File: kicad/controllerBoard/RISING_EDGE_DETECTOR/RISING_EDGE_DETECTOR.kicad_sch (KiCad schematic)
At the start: 10 parts, among them Q385 PMOS, Q386 NMOS, Q391 PMOS, Q392 NMOS, Q393 PMOS, Q394 NMOS

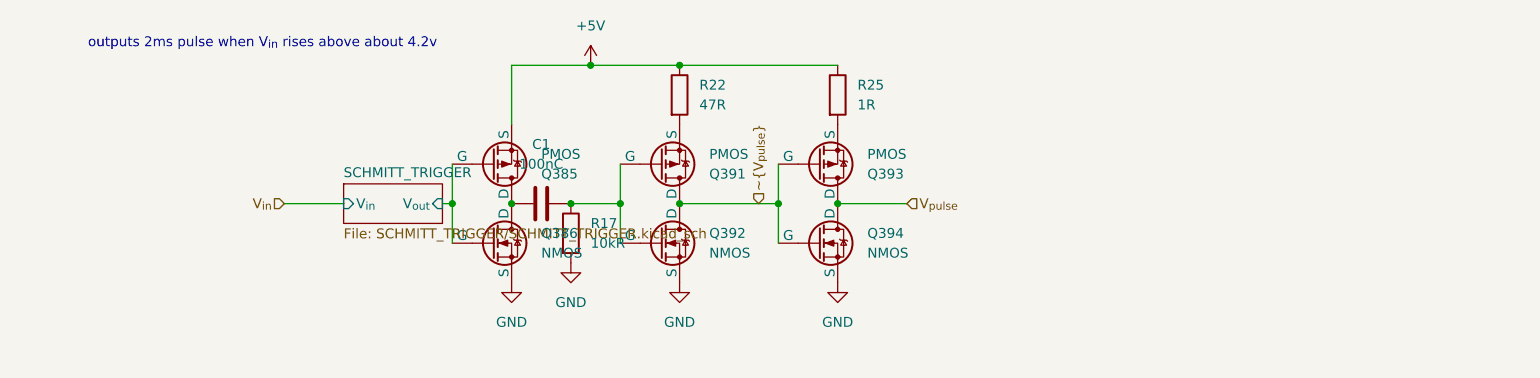
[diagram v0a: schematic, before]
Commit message: simulate rc pulses
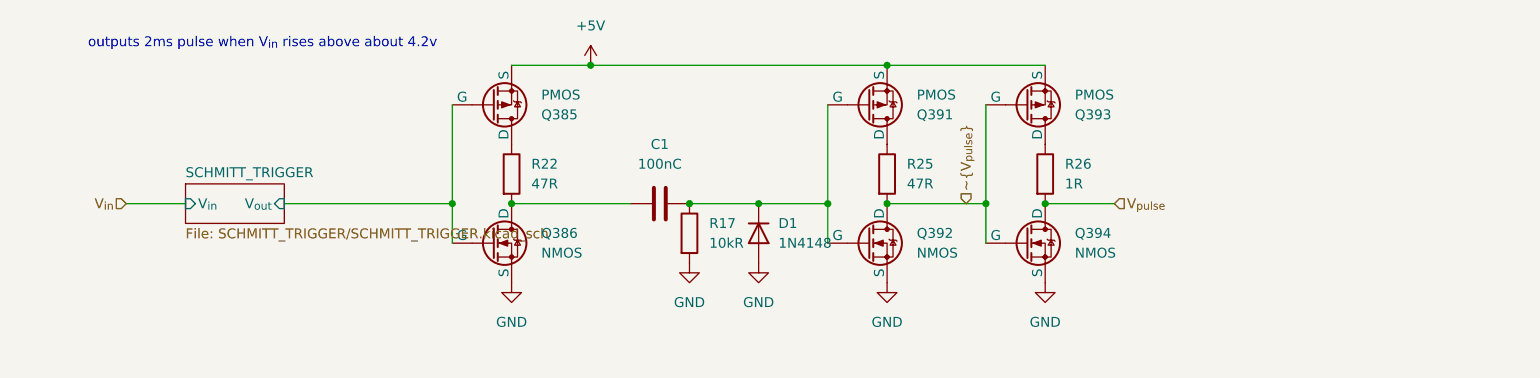
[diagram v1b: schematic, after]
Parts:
- added D1: 1N4148, Diode_THT:D_DO-35_SOD27_P7.62mm_Horizontal, symbol Diode:1N4148
- added R26: 1R, symbol Device:R
- R25: value 1R -> 47R
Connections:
- net +5V: now also Q391.3 (S), Q393.3 (S); no longer R22.1, R25.1
- net GND: now also D1.2 (A)
- net V_{pulse}: now also R26.2; no longer Q393.1 (D)
- net ~{V_{pulse}}: now also R25.2; no longer Q391.1 (D)
- net at C1.1, Q386.1 (D): now also R22.2; no longer Q385.1 (D)
- net at C1.2, Q391.2 (G), Q392.2 (G)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: now also D1.1 (K)
- new net: Q391.1 (D), R25.1
- new net: Q385.1 (D), R22.1
- new net: Q393.1 (D), R26.1
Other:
- moved on the sheet: C1, Q392, Q394, R17

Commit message: finish main schematic
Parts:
- added Q425: PMOS, symbol Simulation_SPICE:PMOS
- added Q426: NMOS, symbol Simulation_SPICE:NMOS
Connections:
- net +5V: now also Q425.3 (S)
- net GND: now also Q426.3 (S)
- net V_{pulse}: now also Q425.2 (G), Q426.2 (G)
- net ~{V_{pulse}}: now also Q425.1 (D), Q426.1 (D); no longer Q392.1 (D), Q393.2 (G), Q394.2 (G), R25.2
- new net: Q392.1 (D), Q393.2 (G), Q394.2 (G), R25.2

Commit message: stuff
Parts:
- added R55: 47R, symbol Device:R
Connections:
- net ~{V_{pulse}}: now also R55.2; no longer Q425.1 (D)
- new net: Q425.1 (D), R55.1
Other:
- moved on the sheet: Q425
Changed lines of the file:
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@@
+	)
+	(junction
+		(at 166.37 66.04)
+		(diameter 0)
+		(color 0 0 0 0)
 	)
 	(junction
@@
 	)
 	(junction
-		(at 166.37 66.04)
-		(diameter 0)
-		(color 0 0 0 0)
-	)
-	(junction
 		(at 157.48 66.04)
 		(diameter 0)
@@
 	(wire
 		(pts
-			(xy 166.37 57.15) (xy 166.37 66.04)
+			(xy 166.37 53.34) (xy 166.37 66.04)
 		)
 		(stroke
@@
 	(wire
 		(pts
-			(xy 81.28 53.34) (xy 81.28 66.04)
+			(xy 173.99 66.04) (xy 173.99 69.85)
 		)
 		(stroke
@@
 	(wire
 		(pts
-			(xy 111.76 66.04) (xy 120.65 66.04)
+			(xy 81.28 53.34) (xy 81.28 66.04)
 		)
 		(stroke
@@
 	(wire
 		(pts
-			(xy 166.37 66.04) (xy 166.37 74.93)
+			(xy 111.76 66.04) (xy 120.65 66.04)
 		)
 		(stroke
@@
 	(wire
 		(pts
-			(xy 173.99 52.07) (xy 173.99 48.26)
-		)
-		(stroke
-			(width 0)
-			(type default)
-		)
-	)
-	(wire
-		(pts
-			(xy 173.99 62.23) (xy 173.99 69.85)
+			(xy 166.37 66.04) (xy 166.37 74.93)
 		)
 		(stroke
@@
 	(symbol
 		(lib_id "Simulation_SPICE:PMOS")
-		(at 171.45 57.15 0)
+		(at 171.45 53.34 0)
 		(mirror x)
 		(unit 1)
@@
 		(dnp no)
 		(property "Reference" "Q425"
-			(at 177.8 58.4201 0)
+			(at 177.8 54.6101 0)
 			(show_name no)
 			(do_not_autoplace no)
@@
 		)
 		(property "Value" "PMOS"
-			(at 177.8 55.8801 0)
+			(at 177.8 52.0701 0)
 			(show_name no)
 			(do_not_autoplace no)
@@
 		)
 		(property "Footprint" ""
-			(at 176.53 59.69 0)
+			(at 176.53 55.88 0)
 			(hide yes)
 			(show_name no)
@@
 		)
 		(property "Datasheet" "https://ngspice.sourceforge.io/docs/ngspice-html-manual/manual.xhtml#cha_MOSFETs"
-			(at 171.45 44.45 0)
+			(at 171.45 40.64 0)
 			(hide yes)
 			(show_name no)
@@
 		)
 		(property "Description" "P-MOSFET transistor, drain/source/gate"
-			(at 171.45 57.15 0)
+			(at 171.45 53.34 0)
 			(hide yes)
 			(show_name no)
@@
 		)
 		(property "Sim.Device" "PMOS"
-			(at 171.45 40.005 0)
+			(at 171.45 36.195 0)
 			(hide yes)
 			(show_name no)
@@
 		)
 		(property "Sim.Type" "VDMOS"
+			(at 171.45 34.29 0)
+			(hide yes)
+			(show_name no)
+			(do_not_autoplace no)
+			(effects
+				(font
+					(size 1.27 1.27)
+				)
+			)
+		)
+		(property "Sim.Pins" "1=D 2=G 3=S"
 			(at 171.45 38.1 0)
-			(hide yes)
-			(show_name no)
-			(do_not_autoplace no)
-			(effects
-				(font
-					(size 1.27 1.27)
-				)
-			)
-		)
-		(property "Sim.Pins" "1=D 2=G 3=S"
-			(at 171.45 41.91 0)
 			(hide yes)
 			(show_name no)
@@
 					(unit 1)
 				)
+			)
+		)
+	)
+	(symbol
+		(lib_id "Device:R")
+		(at 173.99 62.23 0)
+		(unit 1)
+		(body_style 1)
+		(exclude_from_sim no)
+		(in_bom yes)
+		(on_board yes)
+		(in_pos_files yes)
+		(dnp no)
+		(fields_autoplaced yes)
+		(property "Reference" "R55"
+			(at 176.53 60.9599 0)
+			(show_name no)
+			(do_not_autoplace no)
+			(effects
+				(font
+					(size 1.27 1.27)
+				)
+				(justify left)
+			)
+		)
+		(property "Value" "47R"
+			(at 176.53 63.4999 0)
+			(show_name no)
+			(do_not_autoplace no)
+			(effects
+				(font
+					(size 1.27 1.27)
+				)
+				(justify left)
+			)
+		)
+		(property "Footprint" ""
+			(at 172.212 62.23 90)
+			(hide yes)
+			(show_name no)
+			(do_not_autoplace no)
+			(effects
+				(font
+					(size 1.27 1.27)
+				)
+			)
+		)
+		(property "Datasheet" ""
+			(at 173.99 62.23 0)
+			(hide yes)
+			(show_name no)
+			(do_not_autoplace no)
+			(effects
+				(font
+					(size 1.27 1.27)
+				)
+			)
+		)
+		(property "Description" "Resistor"
+			(at 173.99 62.23 0)
+			(hide yes)
+			(show_name no)
+			(do_not_autoplace no)
+			(effects
+				(font
+					(size 1.27 1.27)
+				)
+			)
+		)
+		(pin "2"
+		)
+		(pin "1"
+		)
+		(instances
+			(project "controllerBoard"
+				(path "/93a9a1ca-4ee5-40da-ab67-92836146c003/96d1d3a9-3ebd-46ac-a2d2-b692fac1af2c"
+					(reference "R55")
+					(unit 1)
+				)
+				(path "/93a9a1ca-4ee5-40da-ab67-92836146c003/def1fdf8-7002-45c6-87e0-28926b899265"
+					(reference "R56")
+					(unit 1)
+				)

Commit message: did stuff
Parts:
- renumbered C1 to C7, D1 to D3, Q385 to Q386, Q386 to Q387, Q391 to Q394, Q392 to Q395, Q393 to Q396, Q394 to Q397, Q425 to Q398, Q426 to Q399, R22 to R23, R17 to R28, R25 to R31, R26 to R32, R55 to R33

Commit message: did more simulation, added bom
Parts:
- renumbered C7 to C3, D3 to D1, Q386 to Q385, Q387 to Q386, Q394 to Q387, Q395 to Q388, Q396 to Q389, Q397 to Q390, Q398 to Q391, Q399 to Q392, R23 to R17, R28 to R18, R31 to R19, R32 to R20, R33 to R21

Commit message: update main board schematic
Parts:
- C3: footprint (none) -> Capacitor_SMD:C_0805_2012Metric
- Q385, Q387, Q389, Q391: value PMOS -> Q_PMOS_GSD; footprint (none) -> easyeda2kicad:SOT-23-P; symbol Simulation_SPICE:PMOS -> Transistor_FET:Q_PMOS_GSD
- Q386, Q388, Q390, Q392: value NMOS -> Q_NMOS_GSD; footprint (none) -> easyeda2kicad:SOT-23-N; symbol Simulation_SPICE:NMOS -> Transistor_FET:Q_NMOS_GSD
- R17, R18, R19, R20, R21: footprint (none) -> Resistor_SMD:R_0805_2012Metric
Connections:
- net +5V: now also Q385.2 (S), Q387.2 (S), Q389.2 (S), Q391.2 (S); no longer Q385.3 (S), Q387.3 (S), Q389.3 (S), Q391.3 (S)
- net GND: now also Q386.2 (S), Q388.2 (S), Q390.2 (S), Q392.2 (S); no longer Q386.3 (S), Q388.3 (S), Q390.3 (S), Q392.3 (S)
- net SCHMITT_TRIGGER/V_{out}: now also Q385.1 (G), Q386.1 (G); no longer Q385.2 (G), Q386.2 (G)
- net V_{pulse}: now also Q390.3 (D), Q391.1 (G), Q392.1 (G); no longer Q390.1 (D), Q391.2 (G), Q392.2 (G)
- net ~{V_{pulse}}: now also Q392.3 (D); no longer Q392.1 (D)
- net at Q387.1 (G): now also C3.2, D1.1 (K), Q388.1 (G), R18.1; no longer R19.1
- net at R17.1: now also Q385.3 (D); no longer Q385.1 (D)
- net at C3.1, R17.2: now also Q386.3 (D); no longer Q386.1 (D)
- net at R21.1: now also Q391.3 (D); no longer Q391.1 (D)
- net at Q389.1 (G): now also Q388.3 (D), Q390.1 (G), R19.2; no longer R20.1
- new net: Q387.3 (D), R19.1
- new net: Q389.3 (D), R20.1
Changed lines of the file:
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@@
+				)
+			)
+			(project "RISING_EDGE_DETECTOR"
+				(path "/aa2cadd3-fea5-4489-81d0-08c5a28f9dde"
+					(reference "#PWR090")
+					(unit 1)
 				)
 			)
@@
 				)
 			)
+			(project "RISING_EDGE_DETECTOR"
+				(path "/aa2cadd3-fea5-4489-81d0-08c5a28f9dde"
+					(reference "#PWR093")
+					(unit 1)
+				)
+			)
 		)
 	)
 	(symbol
-		(lib_id "Simulation_SPICE:NMOS")
+		(lib_id "Transistor_FET:Q_NMOS_GSD")
 		(at 154.94 71.12 0)
 		(unit 1)
@@
 			)
 		)
-		(property "Value" "NMOS"
+		(property "Value" "Q_NMOS_GSD"
 			(at 161.29 72.3899 0)
 			(show_name no)
@@
 			)
 		)
-		(property "Footprint" ""
+		(property "Footprint" "easyeda2kicad:SOT-23-N"
 			(at 160.02 68.58 0)
 			(hide yes)
@@
 				)
 			)
+			(project "RISING_EDGE_DETECTOR"
+				(path "/aa2cadd3-fea5-4489-81d0-08c5a28f9dde"
+					(reference "Q390")
+					(unit 1)
+				)
+			)
 		)
 	)
 	(symbol
-		(lib_id "Simulation_SPICE:PMOS")
+		(lib_id "Transistor_FET:Q_PMOS_GSD")
 		(at 134.62 53.34 0)
 		(mirror x)
@@
 			)
 		)
-		(property "Value" "PMOS"
+		(property "Value" "Q_PMOS_GSD"
 			(at 140.97 52.0701 0)
 			(show_name no)
@@
 			)
 		)
-		(property "Footprint" ""
+		(property "Footprint" "easyeda2kicad:SOT-23-P"
 			(at 139.7 55.88 0)
 			(hide yes)
@@
 				(path "/93a9a1ca-4ee5-40da-ab67-92836146c003/def1fdf8-7002-45c6-87e0-28926b899265"
 					(reference "Q617")
+					(unit 1)
+				)
+			)
+			(project "RISING_EDGE_DETECTOR"
+				(path "/aa2cadd3-fea5-4489-81d0-08c5a28f9dde"
+					(reference "Q387")
 					(unit 1)
 				)
@@
 			)
 		)
-		(property "Footprint" ""
+		(property "Footprint" "Resistor_SMD:R_0805_2012Metric"
 			(at 87.122 62.23 90)
 			(hide yes)
@@
 				(path "/93a9a1ca-4ee5-40da-ab67-92836146c003/def1fdf8-7002-45c6-87e0-28926b899265"
 					(reference "R34")
+					(unit 1)
+				)
+			)
+			(project "RISING_EDGE_DETECTOR"
+				(path "/aa2cadd3-fea5-4489-81d0-08c5a28f9dde"
+					(reference "R17")
 					(unit 1)
 				)
@@
 				)
 			)
+			(project "RISING_EDGE_DETECTOR"
+				(path "/aa2cadd3-fea5-4489-81d0-08c5a28f9dde"
+					(reference "#PWR088")
+					(unit 1)
+				)
+			)
 		)
 	)
@@
 				)
 			)
+			(project "RISING_EDGE_DETECTOR"
+				(path "/aa2cadd3-fea5-4489-81d0-08c5a28f9dde"
+					(reference "#PWR092")
+					(unit 1)
+				)
+			)
 		)
 	)
@@
 			)
 		)
-		(property "Footprint" ""
+		(property "Footprint" "Capacitor_SMD:C_0805_2012Metric"
 			(at 111.76 65.0748 0)
 			(hide yes)
@@
 				)
 			)
+			(project "RISING_EDGE_DETECTOR"
+				(path "/aa2cadd3-fea5-4489-81d0-08c5a28f9dde"
+					(reference "C3")
+					(unit 1)
+				)
+			)
 		)
 	)
 	(symbol
-		(lib_id "Simulation_SPICE:PMOS")
+		(lib_id "Transistor_FET:Q_PMOS_GSD")
 		(at 171.45 53.34 0)
 		(mirror x)
@@
 			)
 		)
-		(property "Value" "PMOS"
+		(property "Value" "Q_PMOS_GSD"
 			(at 177.8 52.0701 0)
 			(show_name no)
@@
 			)
 		)
-		(property "Footprint" ""
+		(property "Footprint" "easyeda2kicad:SOT-23-P"
 			(at 176.53 55.88 0)
 			(hide yes)
@@
 				(path "/93a9a1ca-4ee5-40da-ab67-92836146c003/def1fdf8-7002-45c6-87e0-28926b899265"
 					(reference "Q621")
+					(unit 1)
+				)
+			)
+			(project "RISING_EDGE_DETECTOR"
+				(path "/aa2cadd3-fea5-4489-81d0-08c5a28f9dde"
+					(reference "Q391")
 					(unit 1)
 				)
@@
 				)
 			)
+			(project "RISING_EDGE_DETECTOR"
+				(path "/aa2cadd3-fea5-4489-81d0-08c5a28f9dde"
+					(reference "D1")
+					(unit 1)
+				)
+			)
 		)
 	)
 	(symbol
-		(lib_id "Simulation_SPICE:NMOS")
+		(lib_id "Transistor_FET:Q_NMOS_GSD")
 		(at 134.62 71.12 0)
 		(unit 1)
@@
 			)
 		)
-		(property "Value" "NMOS"
+		(property "Value" "Q_NMOS_GSD"
 			(at 140.97 72.3899 0)
 			(show_name no)
@@
 			)
 		)
-		(property "Footprint" ""
+		(property "Footprint" "easyeda2kicad:SOT-23-N"
 			(at 139.7 68.58 0)
 			(hide yes)
@@
 				)
 			)
+			(project "RISING_EDGE_DETECTOR"
+				(path "/aa2cadd3-fea5-4489-81d0-08c5a28f9dde"
+					(reference "Q388")
+					(unit 1)
+				)
+			)
 		)
 	)
 	(symbol
-		(lib_id "Simulation_SPICE:PMOS")
+		(lib_id "Transistor_FET:Q_PMOS_GSD")
 		(at 154.94 53.34 0)
 		(mirror x)
@@
 			)
 		)
-		(property "Value" "PMOS"
+		(property "Value" "Q_PMOS_GSD"
 			(at 161.29 52.0701 0)
 			(show_name no)
@@
 			)
 		)
-		(property "Footprint" ""
+		(property "Footprint" "easyeda2kicad:SOT-23-P"
 			(at 160.02 55.88 0)
 			(hide yes)
@@
 				(path "/93a9a1ca-4ee5-40da-ab67-92836146c003/def1fdf8-7002-45c6-87e0-28926b899265"
 					(reference "Q619")
+					(unit 1)
+				)
+			)
+			(project "RISING_EDGE_DETECTOR"
+				(path "/aa2cadd3-fea5-4489-81d0-08c5a28f9dde"
+					(reference "Q389")
 					(unit 1)
 				)
@@
 				)
 			)
+			(project "RISING_EDGE_DETECTOR"
+				(path "/aa2cadd3-fea5-4489-81d0-08c5a28f9dde"
+					(reference "#PWR087")
+					(unit 1)
+				)
+			)
 		)
 	)
 	(symbol
-		(lib_id "Simulation_SPICE:NMOS")
+		(lib_id "Transistor_FET:Q_NMOS_GSD")
 		(at 171.45 74.93 0)
 		(unit 1)
@@
 			)
 		)
-		(property "Value" "NMOS"
+		(property "Value" "Q_NMOS_GSD"
 			(at 177.8 76.1999 0)
 			(show_name no)
@@
 			)
 		)
-		(property "Footprint" ""
+		(property "Footprint" "easyeda2kicad:SOT-23-N"
 			(at 176.53 72.39 0)
 			(hide yes)
@@
 				(path "/93a9a1ca-4ee5-40da-ab67-92836146c003/def1fdf8-7002-45c6-87e0-28926b899265"
 					(reference "Q622")
+					(unit 1)
+				)
+			)
+			(project "RISING_EDGE_DETECTOR"
+				(path "/aa2cadd3-fea5-4489-81d0-08c5a28f9dde"
+					(reference "Q392")
 					(unit 1)
 				)
@@
 			)
 		)
-		(property "Footprint" ""
+		(property "Footprint" "Resistor_SMD:R_0805_2012Metric"
 			(at 155.702 62.23 90)
 			(hide yes)
@@
 				(path "/93a9a1ca-4ee5-40da-ab67-92836146c003/def1fdf8-7002-45c6-87e0-28926b899265"
 					(reference "R37")
+					(unit 1)
+				)
+			)
+			(project "RISING_EDGE_DETECTOR"
+				(path "/aa2cadd3-fea5-4489-81d0-08c5a28f9dde"
+					(reference "R20")
 					(unit 1)
 				)
@@
 			)
 		)
-		(property "Footprint" ""
+		(property "Footprint" "Resistor_SMD:R_0805_2012Metric"
 			(at 109.982 69.85 90)
 			(hide yes)
@@
 				(path "/93a9a1ca-4ee5-40da-ab67-92836146c003/def1fdf8-7002-45c6-87e0-28926b899265"
 					(reference "R35")
+					(unit 1)
+				)
+			)
+			(project "RISING_EDGE_DETECTOR"
+				(path "/aa2cadd3-fea5-4489-81d0-08c5a28f9dde"
+					(reference "R18")
 					(unit 1)
 				)
@@
 			)
 		)
-		(property "Footprint" ""
+		(property "Footprint" "Resistor_SMD:R_0805_2012Metric"
 			(at 135.382 62.23 90)
 			(hide yes)
@@
 				(path "/93a9a1ca-4ee5-40da-ab67-92836146c003/def1fdf8-7002-45c6-87e0-28926b899265"
 					(reference "R36")
+					(unit 1)
+				)
+			)
+			(project "RISING_EDGE_DETECTOR"
+				(path "/aa2cadd3-fea5-4489-81d0-08c5a28f9dde"
+					(reference "R19")
 					(unit 1)
 				)
@@
 				)
 			)
+			(project "RISING_EDGE_DETECTOR"
+				(path "/aa2cadd3-fea5-4489-81d0-08c5a28f9dde"
+					(reference "#PWR089")
+					(unit 1)
+				)
+			)
 		)
 	)
 	(symbol
-		(lib_id "Simulation_SPICE:PMOS")
+		(lib_id "Transistor_FET:Q_PMOS_GSD")
 		(at 86.36 53.34 0)
 		(mirror x)
@@
 			)
 		)
-		(property "Value" "PMOS"
+		(property "Value" "Q_PMOS_GSD"
 			(at 92.71 52.0701 0)
 			(show_name no)
@@
 			)
 		)
-		(property "Footprint" ""
+		(property "Footprint" "easyeda2kicad:SOT-23-P"
 			(at 91.44 55.88 0)
 			(hide yes)
@@
 				(path "/93a9a1ca-4ee5-40da-ab67-92836146c003/def1fdf8-7002-45c6-87e0-28926b899265"
 					(reference "Q615")
+					(unit 1)
+				)
+			)
+			(project "RISING_EDGE_DETECTOR"
+				(path "/aa2cadd3-fea5-4489-81d0-08c5a28f9dde"
+					(reference "Q385")
 					(unit 1)
 				)
@@
 			)
 		)
-		(property "Footprint" ""
+		(property "Footprint" "Resistor_SMD:R_0805_2012Metric"
 			(at 172.212 62.23 90)
 			(hide yes)
@@
 				(path "/93a9a1ca-4ee5-40da-ab67-92836146c003/def1fdf8-7002-45c6-87e0-28926b899265"
 					(reference "R38")
+					(unit 1)
+				)
+			)
+			(project "RISING_EDGE_DETECTOR"
+				(path "/aa2cadd3-fea5-4489-81d0-08c5a28f9dde"
+					(reference "R21")
 					(unit 1)
 				)
@@
 				)
 			)
+			(project "RISING_EDGE_DETECTOR"
+				(path "/aa2cadd3-fea5-4489-81d0-08c5a28f9dde"
+					(reference "#PWR091")
+					(unit 1)
+				)
+			)
 		)
 	)
 	(symbol
-		(lib_id "Simulation_SPICE:NMOS")
+		(lib_id "Transistor_FET:Q_NMOS_GSD")
 		(at 86.36 71.12 0)
 		(unit 1)
@@
 			)
 		)
-		(property "Value" "NMOS"
+		(property "Value" "Q_NMOS_GSD"
 			(at 92.71 72.3899 0)
 			(show_name no)
@@
 			)
 		)
-		(property "Footprint" ""
+		(property "Footprint" "easyeda2kicad:SOT-23-N"
 			(at 91.44 68.58 0)
 			(hide yes)
@@
 				(path "/93a9a1ca-4ee5-40da-ab67-92836146c003/def1fdf8-7002-45c6-87e0-28926b899265"
 					(reference "Q616")
+					(unit 1)
+				)
+			)
+			(project "RISING_EDGE_DETECTOR"
+				(path "/aa2cadd3-fea5-4489-81d0-08c5a28f9dde"
+					(reference "Q386")
 					(unit 1)
 				)
@@
 				)
 			)
-		)
-	)
+			(project "RISING_EDGE_DETECTOR"
+				(path "/aa2cadd3-fea5-4489-81d0-08c5a28f9dde"
+					(page "2")
+				)
+			)
+		)
+	)
+	(sheet_instances
+		(path "/"
+			(page "1")
+		)
+	)

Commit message: finished routing all sub schematics
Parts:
- added C4, C5: 100nC, Capacitor_SMD:C_0805_2012Metric, symbol Device:C
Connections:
- net +5V: now also C4.2, C5.2
- net GND: now also C4.1, C5.1
